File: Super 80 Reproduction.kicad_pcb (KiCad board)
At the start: 2 copper layers, 305 x 310.5 mm, 318 parts, among them J1 8 PIN HEADER, J2 7 PIN HEADER, J3 10 PIN HEADER, J4 2 PIN HEADER, J5 S-100 CONNECTOR, J6 KEYBOARD CONNECTOR, Q1 BC548, Q2 BC327, SW1 4-WAY DIP SWITCH, SW2 4-WAY DIP SWITCH, SW3 PCB MOM SW 2-PIN, U1 LM311, U10 81LS95, U11 74LS30, U12 81LS95, U13 81LS95, U14 74LS00, U15 74LS04, U16 74LS14, U17 74121, U18 74LS174, U2 7905T, U20 74157, U21 74157, U22 74LS04, U23 74LS165, U25 74109, U26 2516 or 2532, U27 2513, U28 74LS00, U29 74LS93, U3 74LS02, U30 74LS86, U31 74LS90, U32 74LS138, U33 2532, U34 74LS374, U35 74LS30, U36 74LS92, U37 74LS00, U38 74LS367, U39 74LS04, U4 81LS95, U40 74LS93, U41 74LS139, U42 2532, U43 74LS367, U44 74109, U45 74LS93, U46 Z80 CPU, U47 Z80 PIO, U48 74LS27, U49 74LS30, U5 81LS95, U50 74LS20, U51 4116, U52 4116, U53 4116, U54 4116, U55 4116, U56 4116, U57 4116, U58 4116, U59 4116, U6 74LS74, U60 4116, U61 4116, U62 4116, U63 4116, U64 4116, U65 4116, U66 4116, U67 4116, U68 4116, U69 4116, U7 74LS02, U70 4116, U71 4116, U72 4116, U73 4116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

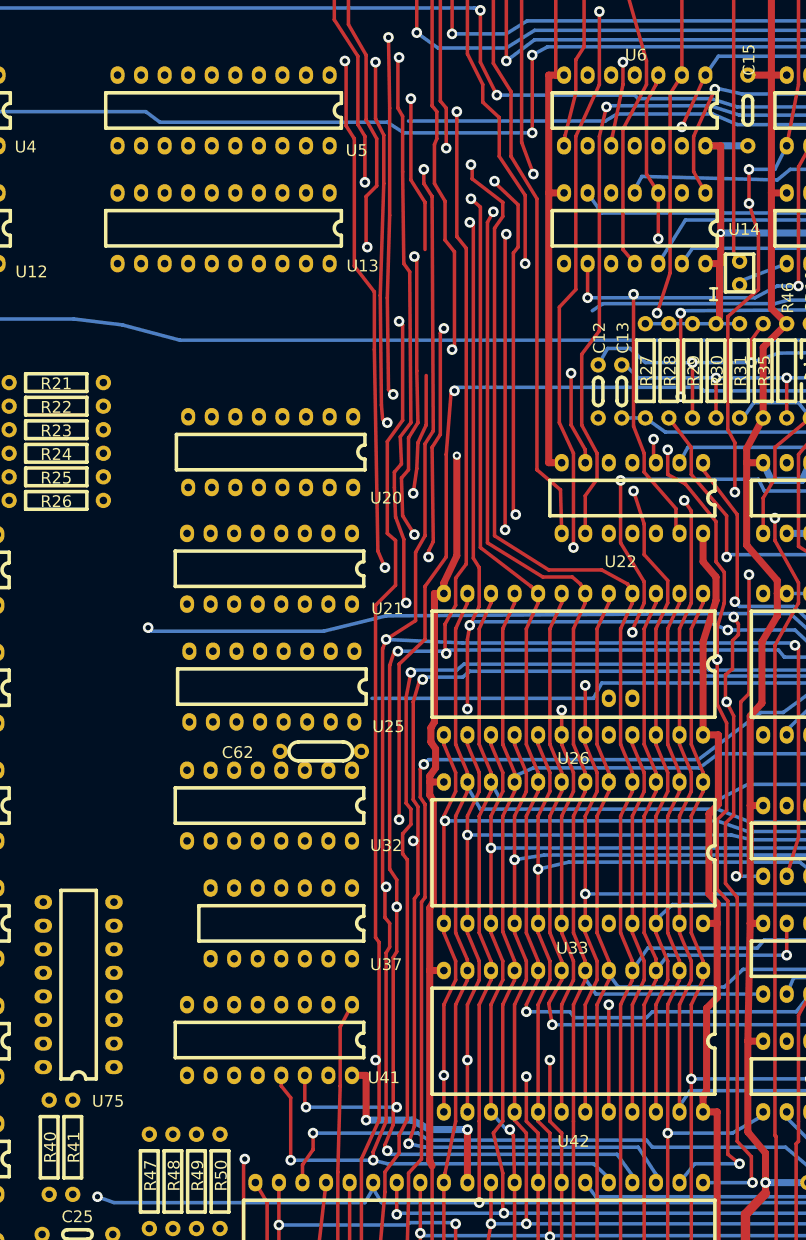
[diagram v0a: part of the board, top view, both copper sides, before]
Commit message: Add files via upload
Added bottom layer traces in the vicinity of the 3 24-pin ICs U26, U33 and U42.
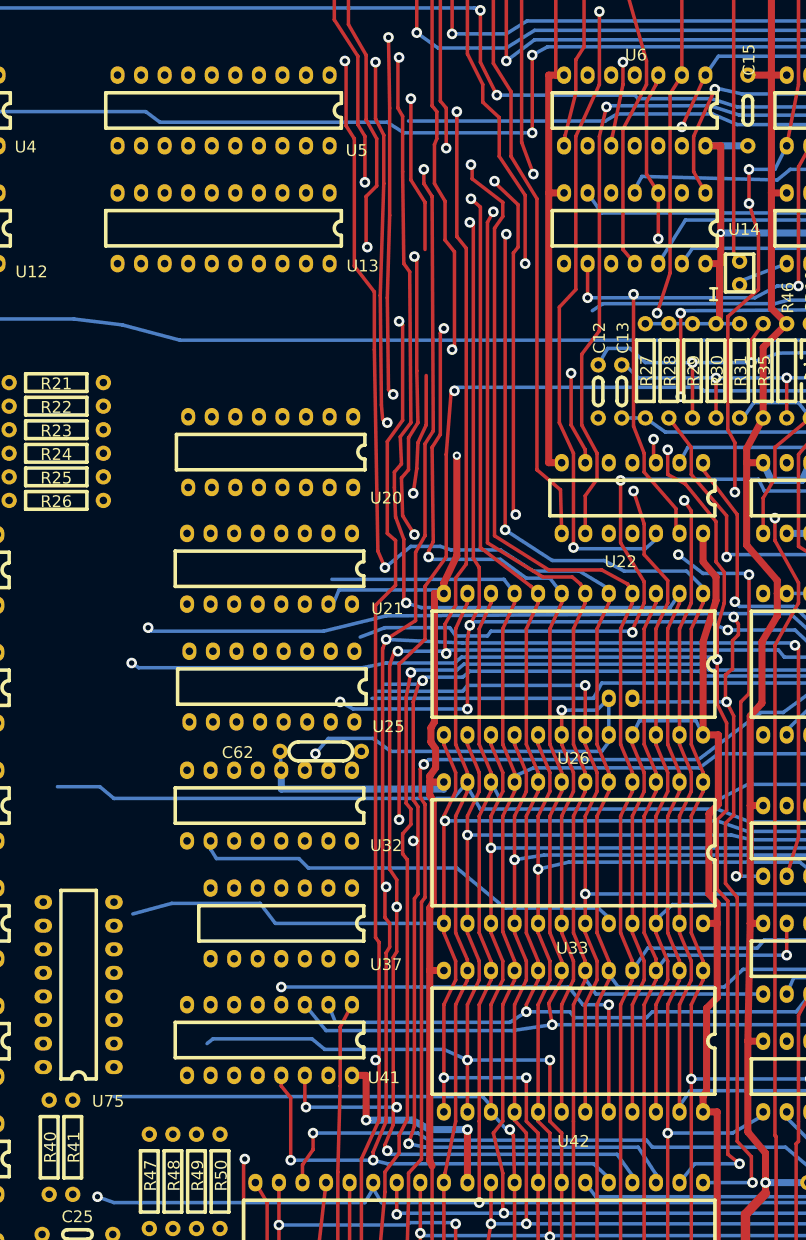
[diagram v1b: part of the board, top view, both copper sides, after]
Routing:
- net /CPU & ROM/A6: track 121.6 -> 212.1 mm, vias 1 -> 3
- net (no net): track 459.6 -> 376.2 mm, vias 22 -> 19
- net /CPU & ROM/A3: track 159.6 -> 242.1 mm, vias 0 -> 2
- net /CPU & ROM/A12: track 224.9 -> 302.6 mm, vias 8 -> 10
- net ROM1*: track 0.00 -> 47.4 mm
- net /CPU & ROM/D2: track 238.1 -> 283.6 mm
- net ROM0*: track 44.4 -> 88.0 mm, vias 1 -> 2
- net /CPU & ROM/D3: track 224.5 -> 268.0 mm
- net /CPU & ROM/D5: track 223.6 -> 265.4 mm
- net /CPU & ROM/D4: track 228.8 -> 266.6 mm
- net ROM2*: track 11.6 -> 47.8 mm, vias 1 -> 2
- net GND: track 957.7 -> 993.9 mm
- net IOREQ-BUFRD*: track 150.3 -> 180.7 mm
- net /CPU & ROM/A1: track 213.9 -> 244.0 mm
- net /CPU & ROM/A7: track 144.0 -> 168.0 mm
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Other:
- net class 30 Power: trace_width 0.381 -> 0.762

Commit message: Add files via upload
Reflects additional PCB traces added on 11.10.2016 (mostly bottom layer in the vicinity of the ICs U6 to U22).
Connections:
- U10 pad 10: (no net) -> GND
- U10 pad 20: (no net) -> VCC
- U12 pad 10: (no net) -> GND
- U12 pad 20: (no net) -> VCC
- U13 pad 10: (no net) -> GND
- U13 pad 20: (no net) -> VCC
- U4 pad 10: (no net) -> GND
- U4 pad 20: (no net) -> VCC
- U5 pad 10: (no net) -> GND
- U5 pad 20: (no net) -> VCC
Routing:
- net (no net): track 376.2 -> 146.6 mm, vias 19 -> 8
- net N-00000362: track 0.00 -> 147.9 mm, vias 0 -> 2
- net N-00000230: track 9.40 -> 121.4 mm, vias 1 -> 2
- net /S-100 Interface/S100-SINTA: track 67.9 -> 175.2 mm, vias 3 -> 4
- net 6LATCH*: track 0.00 -> 96.6 mm, vias 0 -> 3
- net VDU-ENABLE: track 99.7 -> 187.3 mm, vias 3 -> 4
- net /CPU & ROM/A12: track 302.6 -> 217.3 mm, vias 10 -> 7
- net N-0000099: track 10.1 -> 94.4 mm
- net VCC: track 863.0 -> 945.2 mm
- net /CPU & ROM/A8: track 135.6 -> 191.7 mm, vias 2 -> 4
- net N-00000232: track 0.00 -> 55.5 mm, vias 0 -> 2
- net MEMREQ-BUFRD*: track 135.1 -> 186.7 mm
- net GND: track 993.9 -> 1043.9 mm, vias 17 -> 18
- net 12MHz*: track 181.4 -> 224.6 mm
- net /CPU & ROM/A1: track 244.0 -> 283.2 mm, vias 4 -> 6
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
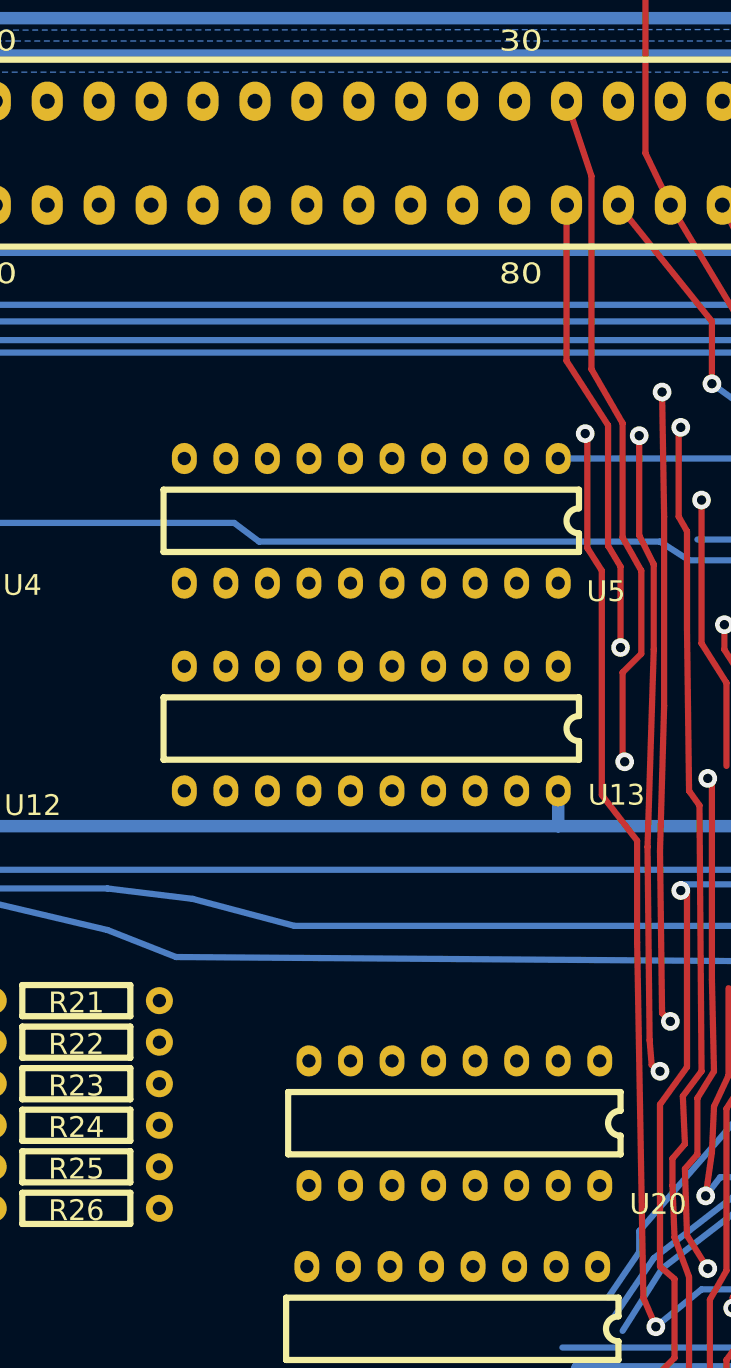
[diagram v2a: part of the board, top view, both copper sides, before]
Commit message: Add files via upload
Added top layer tracks in the vicinity of U5 and U13.
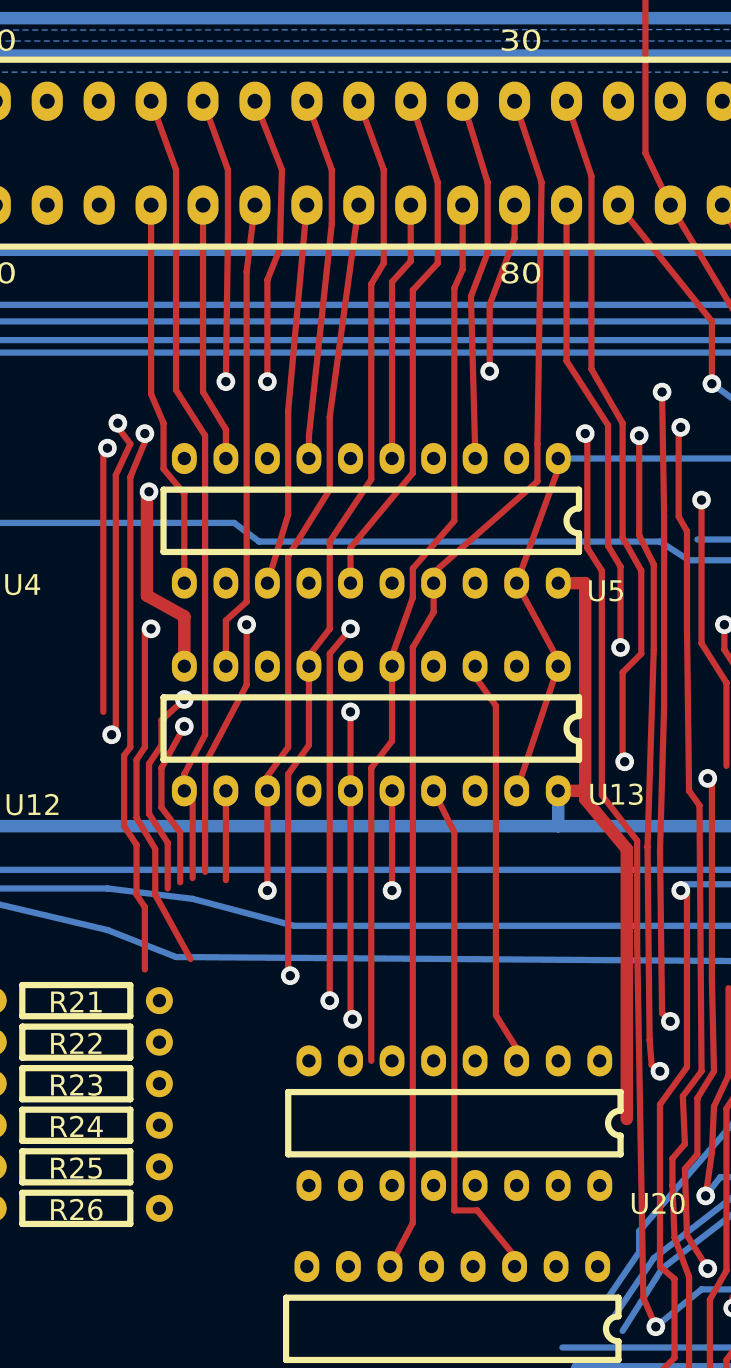
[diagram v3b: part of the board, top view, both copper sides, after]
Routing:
- net (no net): track 146.6 -> 304.6 mm, vias 8 -> 19
- net /RAM/S100-A4: track 0.00 -> 75.1 mm
- net /RAM/S100-A12: track 0.00 -> 55.7 mm, vias 0 -> 1
- net /RAM/S100-A2: track 0.00 -> 54.0 mm
- net /RAM/S100-A10: track 0.00 -> 49.1 mm
- net /RAM/S100-A7: track 0.00 -> 43.2 mm, vias 0 -> 1
- net VCC: track 945.2 -> 982.2 mm
- net GND: track 1043.9 -> 1077.8 mm, vias 18 -> 19
- net /S-100 Interface/S100-A15: track 0.00 -> 31.7 mm
- net /RAM/S100-A5: track 42.0 -> 73.6 mm
- net /RAM/S100-A13: track 0.00 -> 28.8 mm
- net /RAM/S100-A0: track 28.0 -> 52.9 mm
- net /RAM/S100-A1: track 0.00 -> 24.5 mm, vias 0 -> 2
- net /RAM/S100-A11: track 0.00 -> 23.7 mm
- net /RAM/S100-A8: track 0.00 -> 23.4 mm
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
